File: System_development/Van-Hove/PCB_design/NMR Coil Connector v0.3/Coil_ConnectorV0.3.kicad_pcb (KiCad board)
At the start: 2 copper layers, 15.5 x 88.9 mm, 7 parts, among them J1 Conn_Coaxial

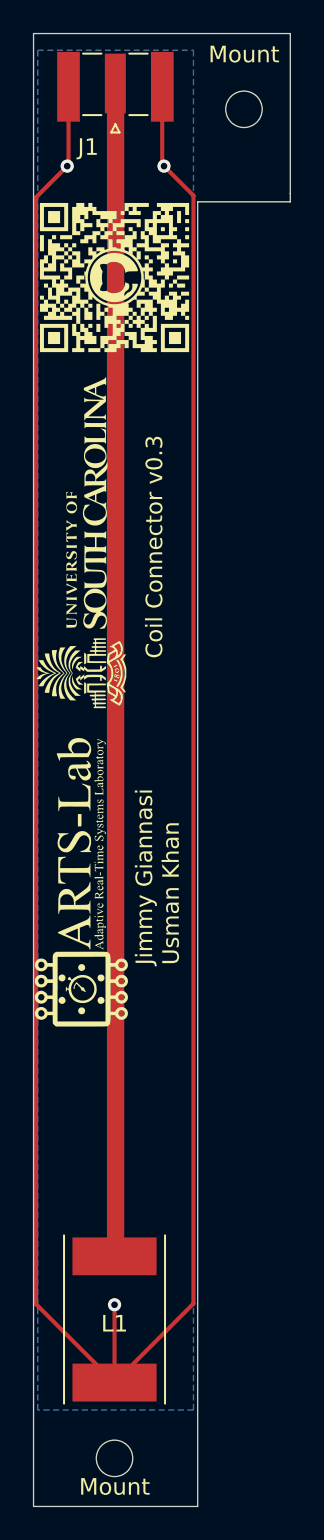
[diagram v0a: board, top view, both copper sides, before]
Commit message: updated traces on coil connector
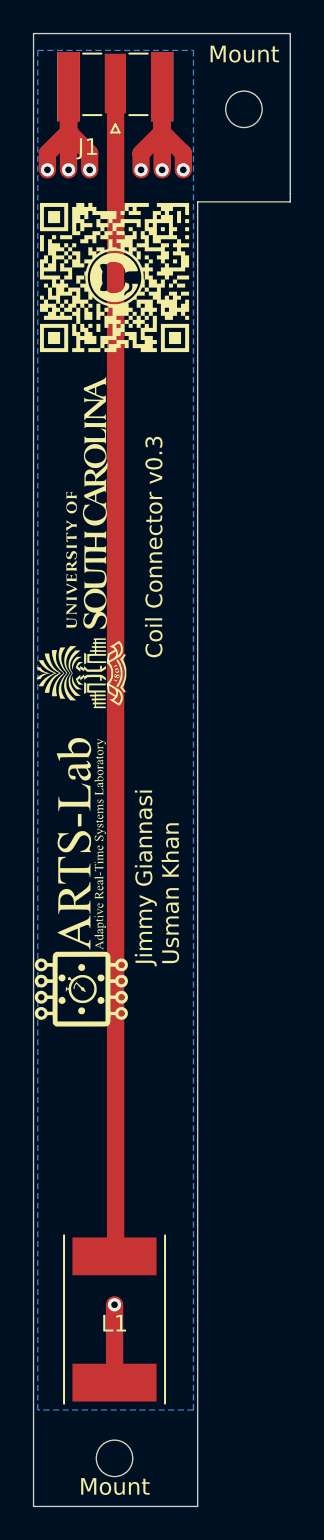
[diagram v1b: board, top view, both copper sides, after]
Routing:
- net GND: track 166.7 -> 34.5 mm, vias 3 -> 7
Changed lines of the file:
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@@
 	)
 	(segment
-		(start 141.986 104.775)
-		(end 143.764 106.553)
+		(start 141.875 102.725)
+		(end 140.6 104)
+		(width 1.044)
+		(layer "F.Cu")
+		(net 1)
+	)
+	(segment
+		(start 137.5 104)
+		(end 137.5 105)
+		(width 1.044)
+		(layer "F.Cu")
+		(net 1)
+	)
+	(segment
+		(start 140.6 104)
+		(end 140.6 105)
+		(width 1.044)
+		(layer "F.Cu")
+		(net 1)
+	)
+	(segment
+		(start 141.875 102.725)
+		(end 143.15 104)
+		(width 1.044)
+		(layer "F.Cu")
+		(net 1)
+	)
+	(segment
+		(start 139 178.199)
+		(end 139 173.5)
+		(width 1.044)
+		(layer "F.Cu")
+		(net 1)
+	)
+	(segment
+		(start 136.225 99.9855)
+		(end 136.225 102.725)
+		(width 1.044)
+		(layer "F.Cu")
+		(net 1)
+	)
+	(segment
+		(start 141.875 99.9855)
+		(end 141.875 102.725)
+		(width 1.044)
+		(layer "F.Cu")
+		(net 1)
+	)
+	(segment
+		(start 136.225 102.725)
+		(end 134.95 104)
+		(width 1.044)
+		(layer "F.Cu")
+		(net 1)
+	)
+	(segment
+		(start 143.15 104)
+		(end 143.15 105)
+		(width 1.044)
+		(layer "F.Cu")
+		(net 1)
+	)
+	(segment
+		(start 136.225 99.9855)
+		(end 136.225 105)
+		(width 1.044)
+		(layer "F.Cu")
+		(net 1)
+	)
+	(segment
+		(start 136 104)
+		(end 136.225 103.775)
 		(width 0.25)
 		(layer "F.Cu")
@@
 	)
 	(segment
-		(start 139 173.5)
-		(end 139 178.199)
-		(width 0.25)
+		(start 134.95 104)
+		(end 134.95 105)
+		(width 1.044)
+		(layer "F.Cu")
+		(net 1)
+	)
+	(segment
+		(start 136.225 102.725)
+		(end 137.5 104)
+		(width 1.044)
+		(layer "F.Cu")
+		(net 1)
+	)
+	(segment
+		(start 141.875 99.9855)
+		(end 141.875 105)
+		(width 1.044)
 		(layer "F.Cu")
 		(net 1)
@@
 	(segment
 		(start 136.225 99.9855)
-		(end 136.225 104.694)
-		(width 0.25)
-		(layer "F.Cu")
-		(net 1)
-	)
-	(segment
-		(start 141.875 99.9855)
-		(end 141.875 104.664)
-		(width 0.25)
-		(layer "F.Cu")
-		(net 1)
-	)
-	(segment
-		(start 134.262 173.461)
-		(end 139 178.199)
-		(width 0.25)
-		(layer "F.Cu")
-		(net 1)
-	)
-	(segment
-		(start 136.144 104.775)
-		(end 134.262 106.657)
-		(width 0.25)
-		(layer "F.Cu")
-		(net 1)
-	)
-	(segment
-		(start 136.225 104.694)
-		(end 136.144 104.775)
-		(width 0.25)
-		(layer "F.Cu")
-		(net 1)
-	)
-	(segment
-		(start 143.764 173.435)
-		(end 139 178.199)
-		(width 0.25)
-		(layer "F.Cu")
-		(net 1)
-	)
-	(segment
-		(start 134.262 106.657)
-		(end 134.262 173.461)
-		(width 0.25)
-		(layer "F.Cu")
-		(net 1)
-	)
-	(segment
-		(start 143.764 106.553)
-		(end 143.764 173.435)
-		(width 0.25)
-		(layer "F.Cu")
-		(net 1)
-	)
-	(segment
-		(start 141.875 104.664)
-		(end 141.986 104.775)
-		(width 0.25)
+		(end 136.225 102.775)
+		(width 1.044)
 		(layer "F.Cu")
 		(net 1)
 	)
 	(via
-		(at 141.986 104.775)
+		(at 140.6 105)
 		(size 0.8)
 		(drill 0.4)
@@
 	)
 	(via
-		(at 136.144 104.775)
+		(at 143.15 105)
+		(size 0.8)
+		(drill 0.4)
+		(layers "F.Cu" "B.Cu")
+		(free yes)
+		(net 1)
+	)
+	(via
+		(at 134.95 105)
+		(size 0.8)
+		(drill 0.4)
+		(layers "F.Cu" "B.Cu")
+		(free yes)
+		(net 1)
+	)
+	(via
+		(at 136.225 105)
+		(size 0.8)
+		(drill 0.4)
+		(layers "F.Cu" "B.Cu")
+		(free yes)
+		(net 1)
+	)
+	(via
+		(at 137.5 105)
 		(size 0.8)
 		(drill 0.4)
@@
 		(size 0.8)
 		(drill 0.4)
+		(layers "F.Cu" "B.Cu")
+		(free yes)
+		(net 1)
+	)
+	(via
+		(at 141.875 105)
+		(size 0.8)
+		(drill 0.4)
